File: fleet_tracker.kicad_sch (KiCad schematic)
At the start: 16 parts, among them J1 DB128V-5.08-5P-GN-S, J2 2685Y-116CNG1SNA01, J3 2685Y-116CNG1SNA01, U2 TJA1051T/3/1J, U3 TSR 1-2450E

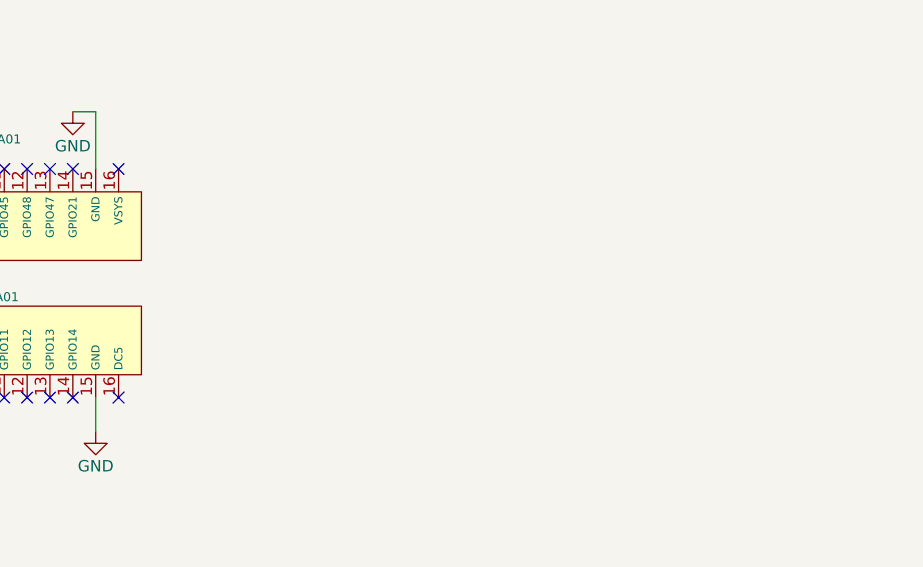
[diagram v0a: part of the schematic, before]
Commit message: sch: add notes about Lilygo board input pins to schematic
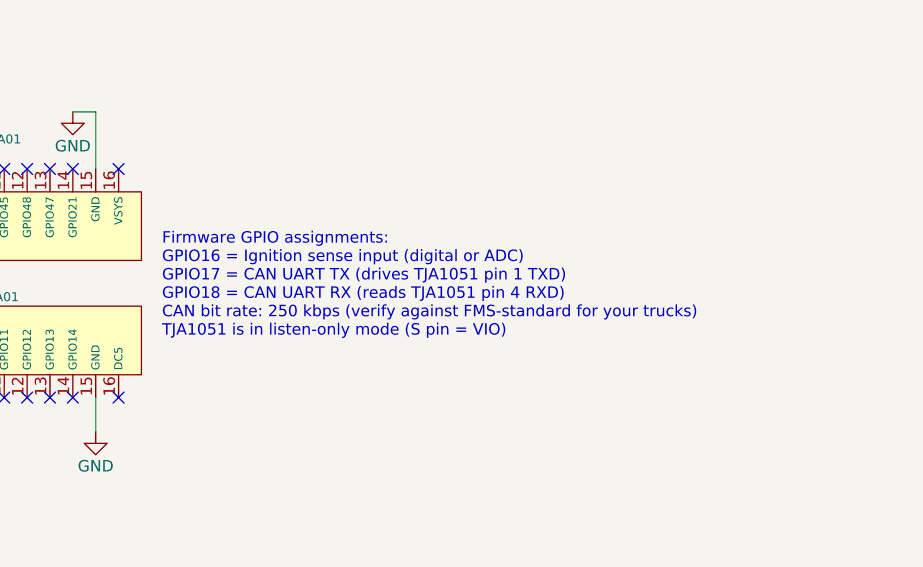
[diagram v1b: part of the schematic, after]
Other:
- note added: "Firmware GPIO assignments: GPIO16 = Ignition sense input (digital or ADC) GPIO17 = CAN UART TX (drives TJA1051 pin 1 TXD) GPIO18 = CAN UART RX (reads TJA1051 pin 4 RXD) CAN bit rate: 250 kbps (verify against FMS-standard for your trucks) TJA1051 is in listen-only mode (S pin = VIO)"
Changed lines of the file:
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@@
 	(generator_version "9.0")
 	(paper "A4")
+	(text "Firmware GPIO assignments:\nGPIO16 = Ignition sense input (digital or ADC)\nGPIO17 = CAN UART TX (drives TJA1051 pin 1 TXD)\nGPIO18 = CAN UART RX (reads TJA1051 pin 4 RXD)\nCAN bit rate: 250 kbps (verify against FMS-standard for your trucks)\nTJA1051 is in listen-only mode (S pin = VIO)"
+		(exclude_from_sim no)
+		(at 243.586 62.484 0)
+		(effects
+			(font
+				(size 1.27 1.27)
+			)
+			(justify left)
+		)
+	)
 	(junction
 		(at 62.23 74.93)

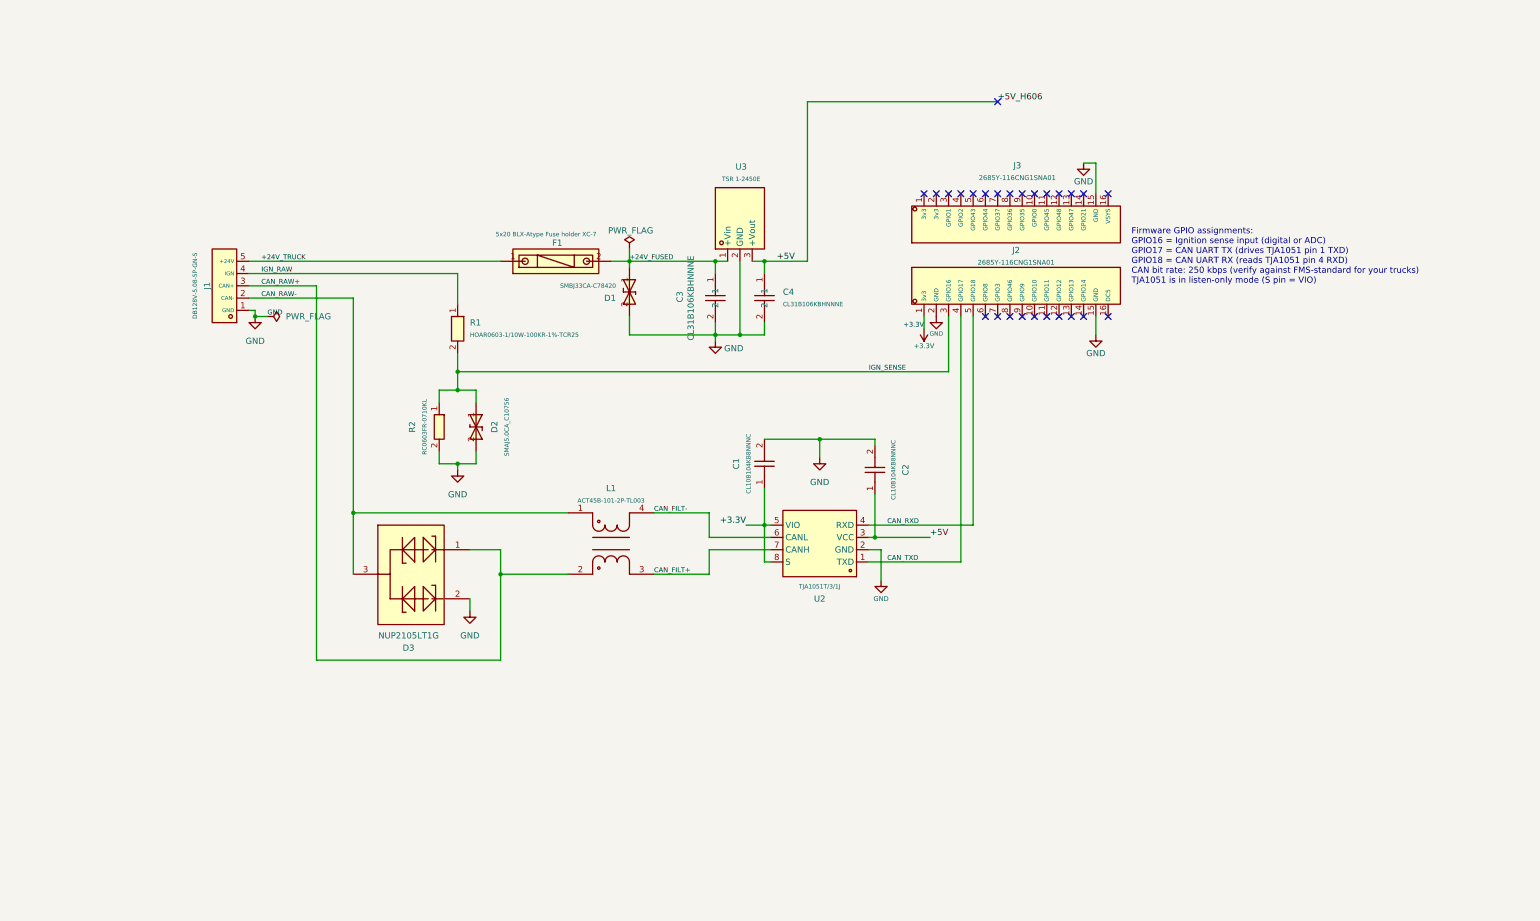
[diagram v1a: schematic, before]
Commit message: sch: make schematic more professional and easier to read
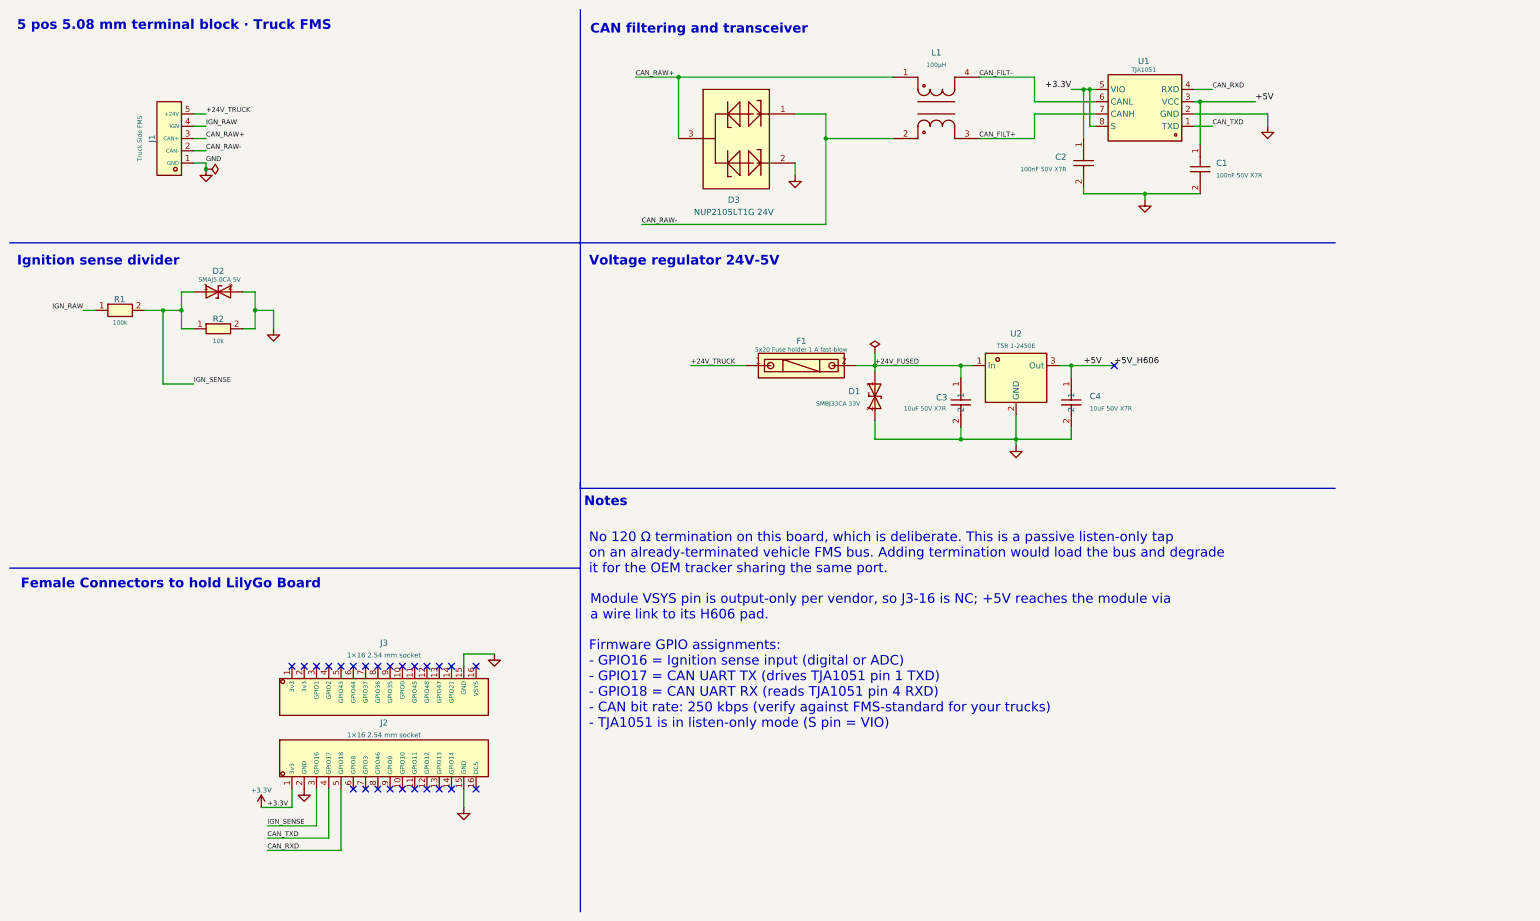
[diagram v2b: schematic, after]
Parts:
- C1, C2: value CL10B104KB8NNNC -> 100nF 50V X7R
- C3, C4: value CL31B106KBHNNNE -> 10uF 50V X7R
- D1: value SMBJ33CA-C78420 -> SMBJ33CA 33V
- D2: value SMAJ5.0CA_C10756 -> SMAJ5.0CA 5V
- D3: value NUP2105LT1G -> NUP2105LT1G 24V
- F1: value 5x20 BLX-Atype Fuse holder XC-7 -> 5x20 Fuse holder 1 A fast-blow
- J1: value DB128V-5.08-5P-GN-S -> Truck Side FMS
- J2, J3: value 2685Y-116CNG1SNA01 -> 1×16 2.54 mm socket
- L1: value ACT45B-101-2P-TL003 -> 100µH
- R1: value HOAR0603-1/10W-100KR-1%-TCR25 -> 100k
- R2: value RC0603FR-0710KL -> 10k
- U1: renamed from U2; value TJA1051T/3/1J -> TJA1051
- renumbered U3 to U2
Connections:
- net +3.3V: now also C2.1; no longer C1.1
- net +5V: now also C1.1; no longer C2.1
- net CAN_RAW+: now also D3.3, L1.1; no longer D3.1, L1.2
- net CAN_RAW-: now also D3.1, L1.2; no longer D3.3, L1.1
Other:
- note added: "5 pos 5.08 mm terminal block · Truck FMS"
- note added: "CAN filtering and transceiver"
- note added: "Female Connectors to hold LilyGo Board"
- note added: "Firmware GPIO assignments: - GPIO16 = Ignition sense input (digital or ADC) - GPIO17 = CAN UART TX (drives TJA1051 pin 1 TXD) - GPIO18 = CAN UART RX (reads TJA1051 pin 4 RXD) - CAN bit rate: 250 kbps (verify against FMS-standard for your trucks) - TJA1051 is in listen-only mode (S pin = VIO)"
- note added: "Ignition sense divider"
- note added: "Module VSYS pin is output-only per vendor, so J3-16 is NC; +5V reaches the module via a wire link to its H606 pad."
- note added: "No 120 Ω termination on this board, which is deliberate. This is a passive listen-only tap on an already-terminated vehicle FMS bus. Adding termination would load the bus and degrade it for the OEM tracker sharing the same port."
- note added: "Notes"
- note added: "Voltage regulator 24V-5V"
- note removed: "Firmware GPIO assignments: GPIO16 = Ignition sense input (digital or ADC) GPIO17 = CAN UART TX (drives TJA1051 pin 1 TXD) GPIO18 = CAN UART RX (reads TJA1051 pin 4 RXD) CAN bit rate: 250 kbps (verify against FMS-standard for your trucks) TJA1051 is in listen-only mode (S pin = VIO)"
- title: (none) -> Fleet Tracker v0
- moved on the sheet: C1, C2, C3, C4, D1, D2, D3, F1, J1, J2, J3, L1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

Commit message: final changes before review
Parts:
- renumbered C2 to C1, C1 to C2
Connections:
- net CAN_RAW+: now also D3.1, L1.2; no longer D3.3, L1.1
- net CAN_RAW-: now also D3.3, L1.1; no longer D3.1, L1.2
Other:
- moved on the sheet: D2, J2, J3, R1, R2
